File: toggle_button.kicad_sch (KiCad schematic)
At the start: 1 part, among them SW1 Push

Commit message: routing done
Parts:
- SW1: footprint mark:BUTTON_XKB_TS-1187A-B-A-B_C318884 -> mark:jlc_pushbutton_wrong_model
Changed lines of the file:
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@@
     (property "Reference" "SW1" (id 0) (at 87.63 37.8292 0))
     (property "Value" "Push" (id 1) (at 87.63 40.3661 0))
-    (property "Footprint" "mark:BUTTON_XKB_TS-1187A-B-A-B_C318884" (id 2) (at 87.63 39.37 0)
+    (property "Footprint" "mark:jlc_pushbutton_wrong_model" (id 2) (at 87.63 39.37 0)
       (effects (font (size 1.27 1.27)) hide)
     )
@@
   (symbol (lib_id "power:VDDF") (at 82.55 44.45 90) (unit 1)
     (in_bom yes) (on_board yes) (fields_autoplaced)
-    (property "Reference" "#PWR013" (id 0) (at 86.36 44.45 0)
+    (property "Reference" "#PWR027" (id 0) (at 86.36 44.45 0)
       (effects (font (size 1.27 1.27)) hide)
     )

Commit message: ready to order
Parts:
- SW1: footprint mark:jlc_pushbutton_wrong_model -> mark:jlc_pushbutton
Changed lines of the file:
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@@
     (property "Reference" "SW1" (id 0) (at 87.63 37.8292 0))
     (property "Value" "Push" (id 1) (at 87.63 40.3661 0))
-    (property "Footprint" "mark:jlc_pushbutton_wrong_model" (id 2) (at 87.63 39.37 0)
+    (property "Footprint" "mark:jlc_pushbutton" (id 2) (at 87.63 39.37 0)
       (effects (font (size 1.27 1.27)) hide)
     )
@@
   (symbol (lib_id "power:VDDF") (at 82.55 44.45 90) (unit 1)
     (in_bom yes) (on_board yes) (fields_autoplaced)
-    (property "Reference" "#PWR027" (id 0) (at 86.36 44.45 0)
+    (property "Reference" "#PWR029" (id 0) (at 86.36 44.45 0)
       (effects (font (size 1.27 1.27)) hide)
     )

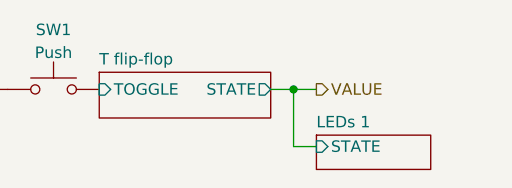
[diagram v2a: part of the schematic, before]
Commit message: started fixing issues from V1
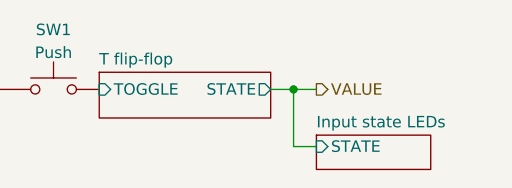
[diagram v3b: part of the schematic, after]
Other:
- sheet LEDs 1 renamed Input state LEDs
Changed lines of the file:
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@@
     (stroke (width 0.1524) (type solid) (color 0 0 0 0))
     (fill (color 0 0 0 0.0000))
-    (property "Sheet name" "LEDs 1" (id 0) (at 116.84 48.8184 0)
+    (property "Sheet name" "Input state LEDs" (id 0) (at 116.84 48.8184 0)
       (effects (font (size 1.27 1.27)) (justify left bottom))
     )

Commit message: pre-re-layout
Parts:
- renumbered SW1 to SW301
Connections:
- net VDDF renamed VDD
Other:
- removed sheet Input state LEDs
- sheet T flip-flop ports: added Q; removed STATE
- note added: "Pushbutton which toggles the output"
- moved on the sheet: SW301
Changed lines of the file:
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@@
 (kicad_sch (version 20211123) (generator eeschema)
-  (paper "A4")
-  (junction (at 114.3 44.45) (diameter 0) (color 0 0 0 0)
-  )
-  (wire (pts (xy 111.76 44.45) (xy 114.3 44.45))
+  (paper "A5")
+  (wire (pts (xy 124.46 90.17) (xy 129.54 90.17))
     (stroke (width 0) (type default) (color 0 0 0 0))
   )
-  (wire (pts (xy 114.3 44.45) (xy 116.84 44.45))
+  (wire (pts (xy 100.33 90.17) (xy 111.125 90.17))
     (stroke (width 0) (type default) (color 0 0 0 0))
   )
-  (wire (pts (xy 114.3 44.45) (xy 114.3 50.8))
+  (wire (pts (xy 85.09 90.17) (xy 90.17 90.17))
     (stroke (width 0) (type default) (color 0 0 0 0))
   )
-  (wire (pts (xy 114.3 50.8) (xy 116.84 50.8))
-    (stroke (width 0) (type default) (color 0 0 0 0))
+  (text "Pushbutton which toggles the output" (at 13.97 19.05 0)
+    (effects (font (size 2.54 2.54) (thickness 0.508) bold) (justify left bottom))
   )
-  (hierarchical_label "VALUE" (shape output) (at 116.84 44.45 0)
+  (hierarchical_label "VALUE" (shape output) (at 129.54 90.17 0)
     (effects (font (size 1.27 1.27)) (justify left))
   )
-  (symbol (lib_id "Switch:SW_Push") (at 87.63 44.45 0) (unit 1)
+  (symbol (lib_id "power:VDD") (at 85.09 90.17 90) (unit 1)
     (in_bom yes) (on_board yes) (fields_autoplaced)
-    (property "Reference" "SW1" (id 0) (at 87.63 37.8292 0))
-    (property "Value" "Push" (id 1) (at 87.63 40.3661 0))
-    (property "Footprint" "mark:jlc_pushbutton" (id 2) (at 87.63 39.37 0)
+    (property "Reference" "#PWR0301" (id 0) (at 88.9 90.17 0)
       (effects (font (size 1.27 1.27)) hide)
     )
-    (property "Datasheet" "https://datasheet.lcsc.com/lcsc/2002271431_XKB-Connectivity-TS-1187A-B-A-B_C318884.pdf" (id 3) (at 87.63 39.37 0)
+    (property "Value" "VDD" (id 1) (at 81.915 90.6038 90)
+      (effects (font (size 1.27 1.27)) (justify left))
+    )
+    (property "Footprint" "" (id 2) (at 85.09 90.17 0)
       (effects (font (size 1.27 1.27)) hide)
     )
-    (property "JLC" "C318884" (id 4) (at 87.63 44.45 0)
+    (property "Datasheet" "" (id 3) (at 85.09 90.17 0)
+      (effects (font (size 1.27 1.27)) hide)
+    )
+    (pin "1")
+  )
+  (symbol (lib_id "Switch:SW_Push") (at 95.25 90.17 0) (unit 1)
+    (in_bom yes) (on_board yes) (fields_autoplaced)
+    (property "Reference" "SW301" (id 0) (at 95.25 83.5492 0))
+    (property "Value" "Push" (id 1) (at 95.25 86.0861 0))
+    (property "Footprint" "mark:jlc_pushbutton" (id 2) (at 95.25 85.09 0)
+      (effects (font (size 1.27 1.27)) hide)
+    )
+    (property "Datasheet" "https://datasheet.lcsc.com/lcsc/2002271431_XKB-Connectivity-TS-1187A-B-A-B_C318884.pdf" (id 3) (at 95.25 85.09 0)
+      (effects (font (size 1.27 1.27)) hide)
+    )
+    (property "JLC" "C318884" (id 4) (at 95.25 90.17 0)
       (effects (font (size 1.27 1.27)) hide)
     )
@@
     (pin "2")
   )
-  (symbol (lib_id "power:VDDF") (at 82.55 44.45 90) (unit 1)
-    (in_bom yes) (on_board yes) (fields_autoplaced)
-    (property "Reference" "#PWR029" (id 0) (at 86.36 44.45 0)
-      (effects (font (size 1.27 1.27)) hide)
+  (sheet (at 111.125 88.265) (size 13.335 4.445) (fields_autoplaced)
+    (stroke (width 0.1524) (type solid) (color 0 0 0 0))
+    (fill (color 0 0 0 0.0000))
+    (property "Sheet name" "T flip-flop" (id 0) (at 111.125 87.5534 0)
+      (effects (font (size 1.27 1.27)) (justify left bottom))
     )
-    (property "Value" "VDDF" (id 1) (at 79.3751 44.8838 90)
+    (property "Sheet file" "t_flip_flop.kicad_sch" (id 1) (at 111.125 93.2946 0)
+      (effects (font (size 1.27 1.27)) (justify left top) hide)
+    )
+    (pin "TOGGLE" input (at 111.125 90.17 180)
       (effects (font (size 1.27 1.27)) (justify left))
     )
-    (property "Footprint" "" (id 2) (at 82.55 44.45 0)
-      (effects (font (size 1.27 1.27)) hide)
-    )
-    (property "Datasheet" "" (id 3) (at 82.55 44.45 0)
-      (effects (font (size 1.27 1.27)) hide)
-    )
-    (pin "1")
-  )
-  (sheet (at 92.71 42.545) (size 19.05 5.08) (fields_autoplaced)
-    (stroke (width 0.1524) (type solid) (color 0 0 0 0))
-    (fill (color 0 0 0 0.0000))
-    (property "Sheet name" "T flip-flop" (id 0) (at 92.71 41.8334 0)
-      (effects (font (size 1.27 1.27)) (justify left bottom))
-    )
-    (property "Sheet file" "t_flip_flop.kicad_sch" (id 1) (at 92.71 48.2096 0)
-      (effects (font (size 1.27 1.27)) (justify left top) hide)
-    )
-    (pin "STATE" output (at 111.76 44.45 0)
+    (pin "Q" output (at 124.46 90.17 0)
       (effects (font (size 1.27 1.27)) (justify right))
     )
-    (pin "TOGGLE" input (at 92.71 44.45 180)
-      (effects (font (size 1.27 1.27)) (justify left))
-    )
   )
-  (sheet (at 116.84 49.53) (size 12.7 3.81) (fields_autoplaced)
-    (stroke (width 0.1524) (type solid) (color 0 0 0 0))
-    (fill (color 0 0 0 0.0000))
-    (property "Sheet name" "Input state LEDs" (id 0) (at 116.84 48.8184 0)
-      (effects (font (size 1.27 1.27)) (justify left bottom))
-    )
-    (property "Sheet file" "state_led.kicad_sch" (id 1) (at 116.84 53.9246 0)
-      (effects (font (size 1.27 1.27)) (justify left top) hide)
-    )
-    (pin "STATE" input (at 116.84 50.8 180)
-      (effects (font (size 1.27 1.27)) (justify left))
-    )
-  )
